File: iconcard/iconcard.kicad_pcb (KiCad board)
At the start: 2 copper layers, 35 x 30.5 mm, 32 parts, among them J1 JST-SH, J3 JST-PH, J4 USB_C_Receptacle_PowerOnly_6P, U1 STM32G030F6Px, U2 KXTJ3-1057, U3 MCP73831-2-OT, U4 AP2112K-3.3

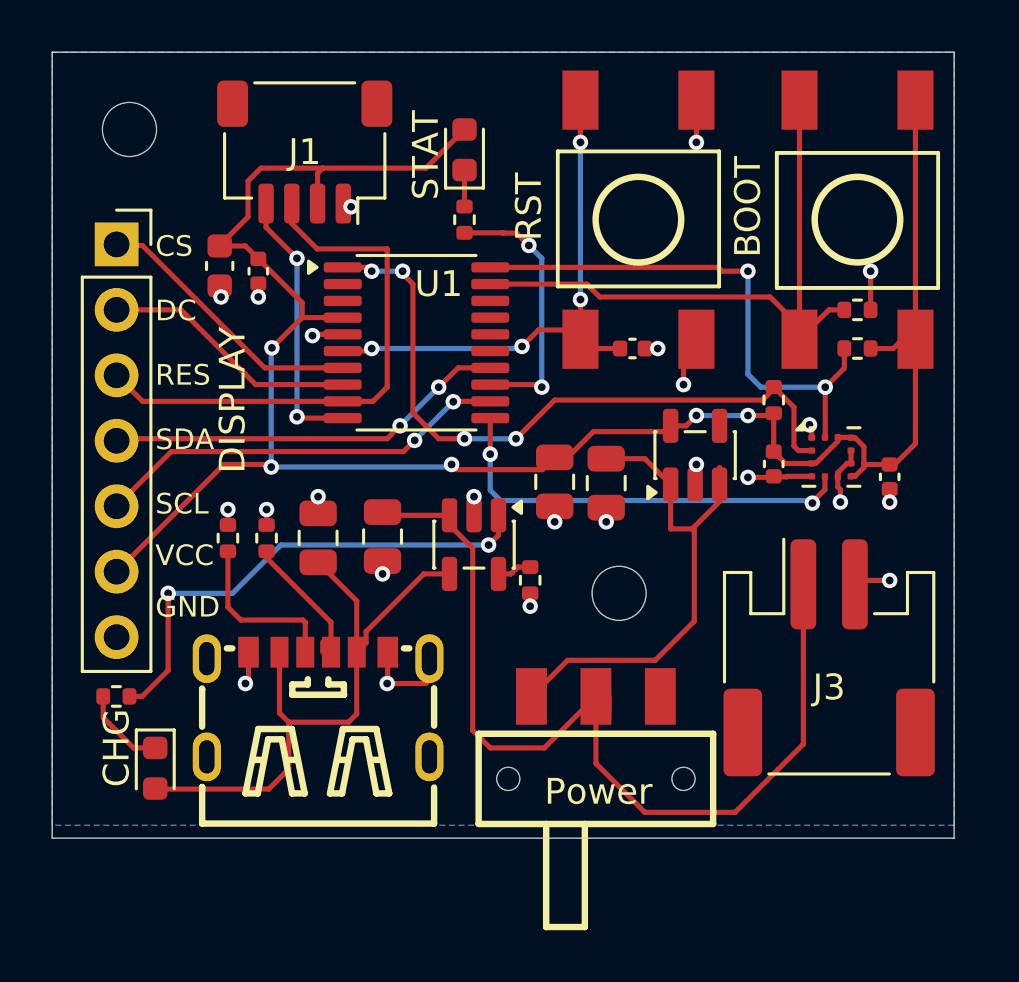
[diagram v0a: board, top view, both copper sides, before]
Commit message: Update tact switch to SKRPACE010, fix LCSC part numbers, add production files
Co-Authored-By: Claude Opus 4.6 <noreply@anthropic.com>
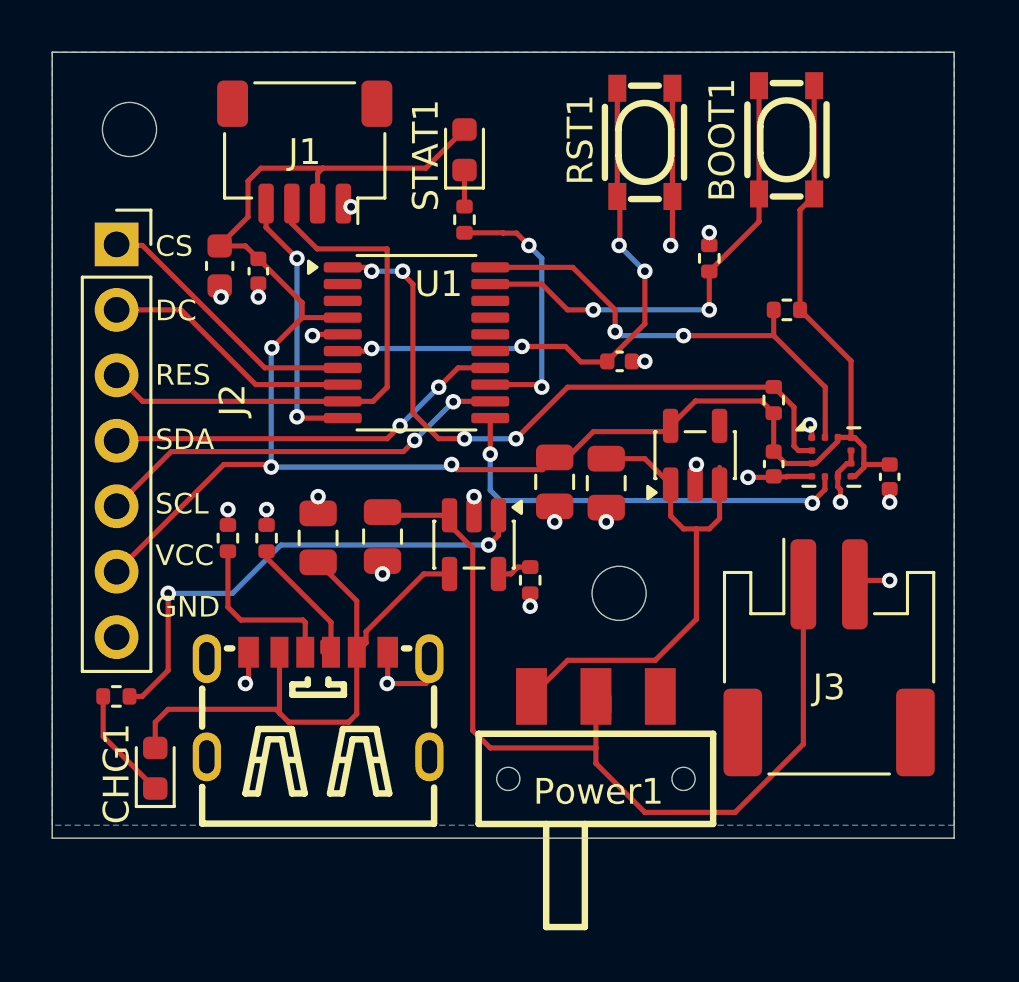
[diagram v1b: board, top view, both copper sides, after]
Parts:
- BOOT1: renamed from BOOT; footprint RST/BOOT (タクトSW):KEY-SMD_4P-L6.0-W6.0-P4.50-LS10.0 -> SKRPACE010:KEY-SMD_4P-L4.2-W3.2-P2.20-LS4.6
- RST1: renamed from RST; footprint RST/BOOT (タクトSW):KEY-SMD_4P-L6.0-W6.0-P4.50-LS10.0 -> SKRPACE010:KEY-SMD_4P-L4.2-W3.2-P2.20-LS4.6
- moved R1 6.09 mm to (44.5, 29.5), turned to 90 degrees
- moved BOOT1 4.14 mm to (47.5, 24.9), turned to 90 degrees
- moved R3 3.12 mm to (47.5, 31.5)
- moved RST1 3.01 mm to (42.0, 25.0), turned to -90 degrees
- moved C3 0.71 mm to (41.0, 33.5)
- turned CHG1 to 90 degrees
- renumbered CHG to CHG1, DISPLAY to J2, Power to Power1, STAT to STAT1
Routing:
- net Net-(U1-PA14/PA15): track 23.7 -> 18.6 mm, vias 0 -> 2
- net Net-(U1-PB3/PB4/PB5/PB6): track 21.0 -> 18.4 mm
- net /VCC: track 79.0 -> 77.6 mm, vias 5 -> 3
- net Net-(CHG1-A): track 24.6 -> 23.3 mm
- net Net-(CHG1-K): track 3.33 -> 4.44 mm
- net Net-(U1-NRST): track 20.7 -> 21.7 mm
- net GND: track 26.2 -> 27.0 mm, vias 24 -> 23
- net Net-(J3-Pin_1): track 37.5 -> 36.7 mm

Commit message: Add BL MOSFET driver, SWD test points, update J2 to 8-pin
Co-Authored-By: Claude Opus 4.6 (1M context) <noreply@anthropic.com>
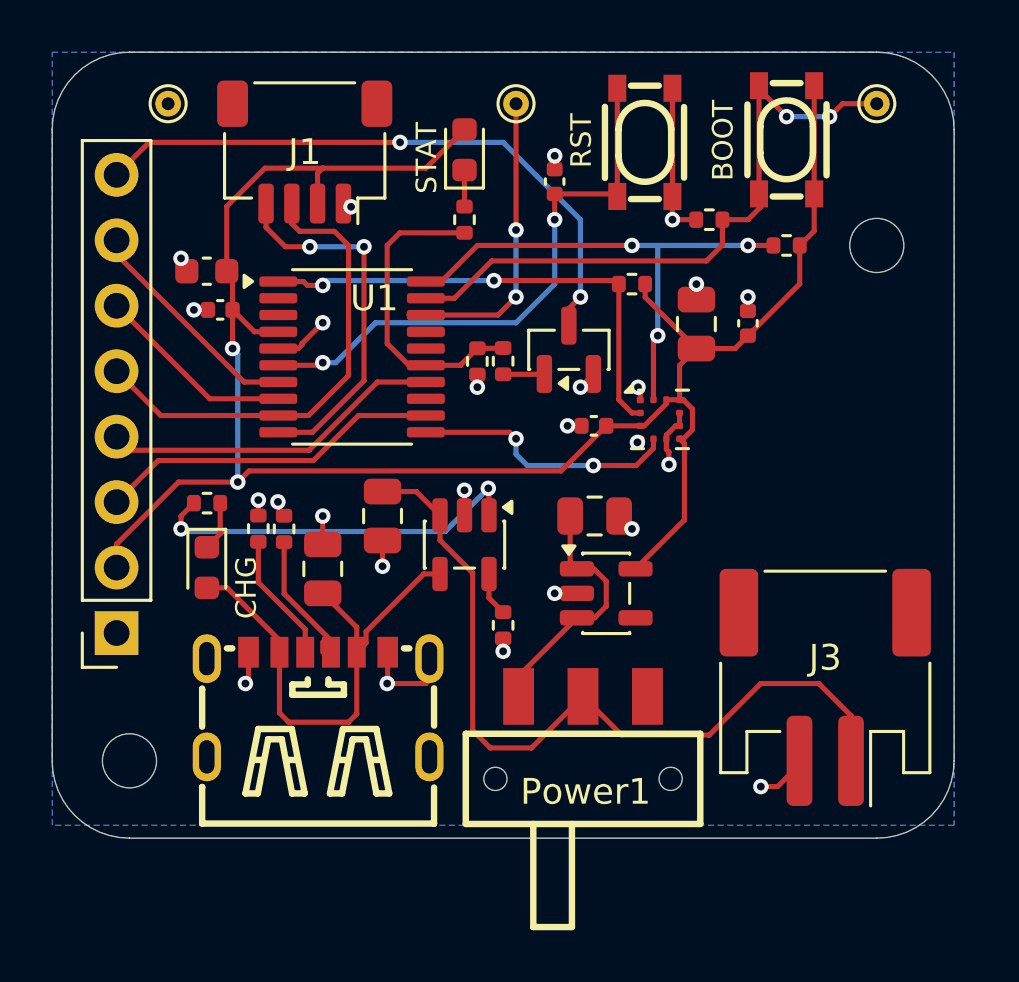
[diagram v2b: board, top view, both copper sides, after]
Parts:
- added Q1: 2N7002, Package_TO_SOT_SMD:SOT-23, F.Cu at (39.0, 33.0)
- added R10: 100K, Resistor_SMD:R_0402_1005Metric, F.Cu at (35.5, 33.5)
- added R9: 100, Resistor_SMD:R_0402_1005Metric, F.Cu at (36.5, 33.5)
- added TP1: SWDIO, TestPoint:TestPoint_THTPad_D1.0mm_Drill0.5mm, F.Cu at (37.0, 23.5)
- added TP2: SWCLK, TestPoint:TestPoint_THTPad_D1.0mm_Drill0.5mm, F.Cu at (51.0, 23.5)
- added TP3: GND, TestPoint:TestPoint_THTPad_D1.0mm_Drill0.5mm, F.Cu at (23.5, 23.5)
- J2: value PinSocket 2.54mm -> Conn_01x08_Socket; footprint Connector_PinSocket_2.54mm:PinSocket_1x07_P2.54mm_Vertical -> Connector_PinSocket_2.54mm:PinSocket_1x08_P2.54mm_Vertical
- R2: value 2K -> 4.7K
- moved REF** 24.5 mm to (22.0, 49.0)
- moved REF** 16.8 mm to (51.0, 29.0)
- moved J2 15.1 mm to (21.5, 44.0), turned to 180 degrees
- moved R8 8.28 mm to (25.0, 39.0), turned to 0 degrees
- moved C9 8.23 mm to (44.0, 32.0), turned to 90 degrees
- moved C7 8.11 mm to (46.0, 32.0), turned to 90 degrees
- moved CHG1 8.04 mm to (25.0, 41.5), turned to -90 degrees
- moved C3 7.42 mm to (38.5, 26.5), turned to 90 degrees
- moved C4 7.14 mm to (40.0, 36.0), turned to 180 degrees
- moved R4 7.11 mm to (41.5, 30.5), turned to 180 degrees
- moved U2 6.81 mm to (42.6, 35.8)
- moved U4 6.38 mm to (40.5, 42.5), turned to 0 degrees
- moved U1 2.56 mm to (30.6, 33.3)
- moved R3 2.50 mm to (47.5, 29.0)
- moved C1 2.11 mm to (25.5, 31.5), turned to 180 degrees
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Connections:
- J2 pad 1: /CS -> GND
- J2 pad 2: /DC -> /VCC
- J2 pad 3: /PA2_TX -> /SCL
- J2 pad 5: /SCL -> /PA2_TX
- J2 pad 6: /VCC -> /DC
- J2 pad 7: GND -> /CS
- R2 pad 2: Net-(U1-PA6) -> Net-(U1-PA8/PB0/PB1/PB2)
- U1 pad 13: Net-(U1-PA6) -> unconnected-(U1-PA6-Pad13)
- U1 pad 15: unconnected-(U1-PA8/PB0/PB1/PB2-Pad15) -> Net-(U1-PA8/PB0/PB1/PB2)
- U1 pad 18: unconnected-(U1-PA13-Pad18) -> /SWDIO
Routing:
- net /BL: track 0.00 -> 24.1 mm, vias 0 -> 2
- net Net-(U1-PA8/PB0/PB1/PB2): track 0.00 -> 12.1 mm
- net /SWDIO: track 0.00 -> 11.4 mm, vias 0 -> 2
- net Net-(U1-PA6): track 10.5 -> 0.00 mm, vias 2 -> 0
- net Net-(Power1-A): track 19.9 -> 10.1 mm
- net Net-(U1-PB7/PB8): track 26.8 -> 19.0 mm, vias 4 -> 2
- net Net-(U1-PA14/PA15): track 18.6 -> 25.3 mm
- net Net-(U1-PA4): track 16.7 -> 10.4 mm
- net Net-(J3-Pin_1): track 36.7 -> 31.0 mm
- net Net-(U3-STAT): track 19.4 -> 14.9 mm
- net Net-(CHG1-A): track 23.3 -> 19.2 mm
- net /PA3_RX: track 10.6 -> 14.5 mm
- net /PA2_TX: track 21.4 -> 18.7 mm
- net Net-(CHG1-K): track 4.44 -> 1.93 mm
- net GND: track 27.0 -> 29.4 mm, vias 23 -> 25
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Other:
- outline, holes or cut-outs redrawn
- board text added: "BL"
- board text added: "BOOT"
- board text added: "CHG"
- board text added: "RST"
- board text added: "STAT"

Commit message: Add README, add Puchi-Pix branding to PCB silkscreen
Co-Authored-By: Claude Opus 4.6 (1M context) <noreply@anthropic.com>
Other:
- board text added: "Puchi-Pix"
- board text added: "by Mizunashi-Lab @yacchin1205"
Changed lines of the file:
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@@
 		(layer "Edge.Cuts")
+	)
+	(gr_text "Puchi-Pix"
+		(at 45 34.5 0)
+		(layer "F.SilkS")
+		(effects
+			(font
+				(size 1 1)
+				(thickness 0.2)
+				(bold yes)
+			)
+			(justify left bottom)
+		)
 	)
 	(gr_text "STAT"
@@
 		)
 	)
+	(gr_text "by Mizunashi-Lab\n@yacchin1205"
+		(at 53 41 0)
+		(layer "F.SilkS")
+		(effects
+			(font
+				(size 0.8 0.8)
+				(thickness 0.1)
+			)
+			(justify right bottom)
+		)
+	)
